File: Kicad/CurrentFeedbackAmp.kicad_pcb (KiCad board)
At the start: 2 copper layers, 200 x 100 mm, 123 parts, among them J1 Test_Etapa_3_Inf, J10 Protecc_Sup_In1, J11 Protecc_Inf_In1, J12 Protecc_Sup_In2, J13 Test_Etapa_3_Inf, J14 Entrada, J15 Salida masa2, J16 Salida tierra, J17 Salida senal, J2 Test_Realim_Out, J3 Salida masa1, J4 Protecc_Sup_Out, J5 Protecc_Inf_Out, J6 Conector Vcc, J7 Conector Vdd, J8 Test_Etapa_3_Inf, J9 Test_Etapa_3_Sup, Q1 TIP42C, Q10 BC858, Q11 BC848, Q12 BC858, Q13 BC559, Q14 BC559, Q15 BC559, Q16 BC549, Q17 BC549, Q18 BC549, Q19 BC559, Q2 BD135, Q20 BC549, Q21 BC559, Q22 BC549, Q23 BC848, Q24 BD136, Q25 BC858, Q26 BC848, Q27 BC848, Q28 BC848, Q29 BC858, Q3 BD136, Q30 BC858, Q31 BC848, Q32 BC858, Q33 BD135, Q34 TIP41C, Q35 BC858, Q36 BC848, Q37 BC848, Q38 BC848, Q4 BC848, Q40 BC858, Q41 BC858, Q5 BC848, Q6 BC858, Q7 BC858, Q8 BC848, Q9 BC858, U1 LM7812_TO220, U2 TL082, U3 LM7912_TO220, U4 LM7805_TO220, U5 LM7905_TO220

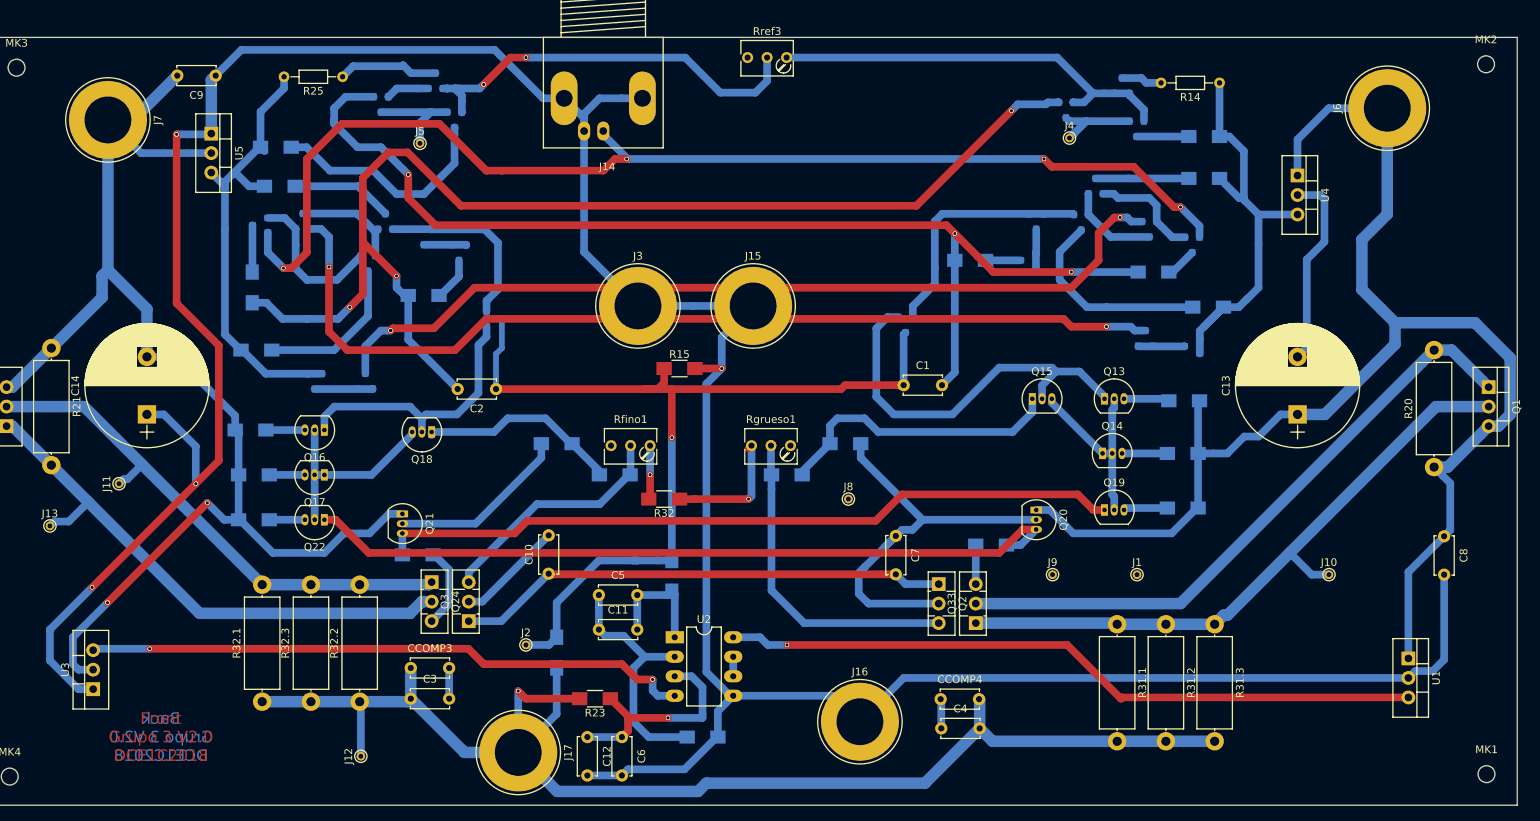
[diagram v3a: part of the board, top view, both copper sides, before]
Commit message: Avance con ensanchado, acomodado de pistas y reposicionamiento de los LM
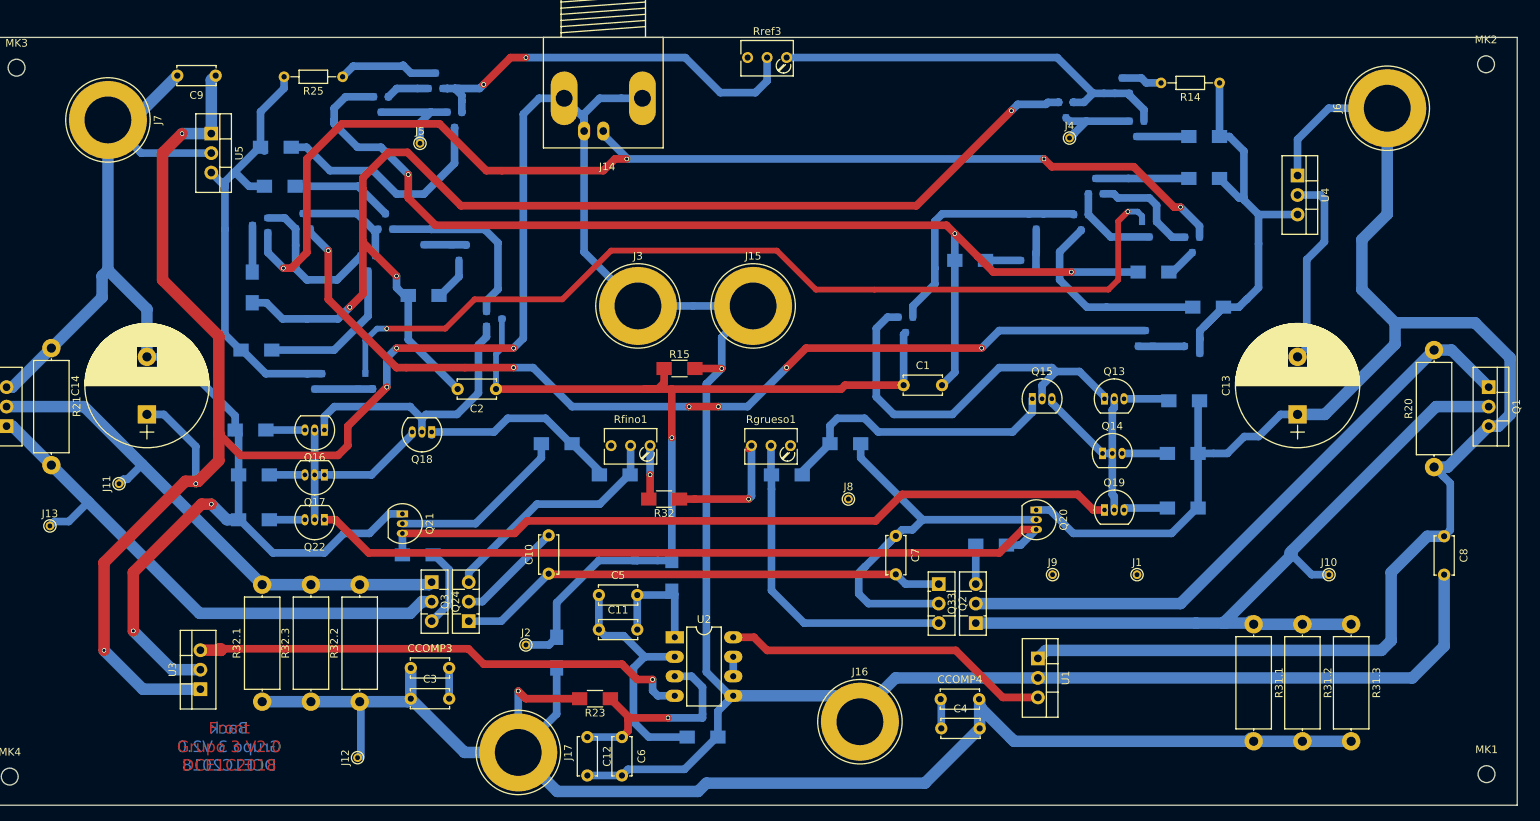
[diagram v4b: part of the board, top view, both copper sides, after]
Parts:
- moved U1 48.3 mm to (140.7, 93.8)
- moved R31.1 17.8 mm to (168.8, 89.3)
- moved R31.2 17.8 mm to (175.1, 89.3)
- moved R31.3 17.8 mm to (181.5, 89.3)
- moved U3 14.0 mm to (31.6, 97.8)
- moved J12 0.47 mm to (52.1, 106.7)
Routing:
- net GND: track 436.7 -> 489.2 mm, vias 4 -> 7
- net VccTL: track 91.3 -> 42.9 mm, vias 1 -> 0
- net Vcc: track 186.7 -> 233.6 mm
- net Vout: track 177.8 -> 197.9 mm
- net Net-(J10-Pad1): track 84.9 -> 103.5 mm
- net VddTL: track 79.2 -> 65.9 mm, vias 2 -> 1
- net Net-(Q12-Pad1): track 114.0 -> 122.1 mm, vias 3 -> 2
- net Net-(Q23-Pad1): track 124.9 -> 126.5 mm, vias 2 -> 6
- net Vdd: track 171.0 -> 171.6 mm

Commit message: Configuracion estrella
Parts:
- R10, R8, R9: moved to F.Cu
- R23: moved to B.Cu
- moved C8 33.1 mm to (183.1, 46.5), turned to 180 degrees
- moved U3 27.4 mm to (58.9, 99.6)
- moved J8 25.8 mm to (141.5, 69.1)
- moved C9 25.8 mm to (29.0, 43.2)
- moved R22 16.7 mm to (99.0, 87.4)
- moved CCOMP3 10.8 mm to (52.8, 103.9), turned to 180 degrees
- moved C3 10.5 mm to (52.8, 107.4), turned to 180 degrees
- moved R15 5.92 mm to (89.4, 59.7)
- moved C4 5.01 mm to (133.1, 102.6), turned to 180 degrees
- moved CCOMP4 5.00 mm to (133.0, 99.1), turned to 180 degrees
- moved J12 4.38 mm to (52.8, 111.0)
- moved R32.2 4.35 mm to (48.0, 98.9)
- moved R32.3 4.35 mm to (41.7, 98.9)
- moved R32.1 4.35 mm to (35.3, 98.9)
- moved J16 3.56 mm to (114.0, 102.9)
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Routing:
- net Net-(C3-Pad2): track 39.3 -> 110.7 mm, vias 0 -> 2
- net Net-(C4-Pad1): track 55.6 -> 119.6 mm, vias 0 -> 1
- net VddTL: track 65.9 -> 37.0 mm
- net Net-(J8-Pad1): track 97.2 -> 109.5 mm
- net GND: track 489.2 -> 480.2 mm, vias 7 -> 1
- net Vout: track 197.9 -> 189.4 mm, vias 1 -> 0
- net Net-(C11-Pad1): track 32.7 -> 24.8 mm
- net Net-(J1-Pad1): track 82.5 -> 87.8 mm
- net Net-(J9-Pad1): track 100.5 -> 105.0 mm
- net Net-(Q23-Pad1): track 126.5 -> 122.3 mm, vias 6 -> 2
- net Vdd: track 171.6 -> 175.1 mm, vias 2 -> 0
- net Net-(R32-Pad2): track 7.03 -> 10.4 mm
- net Ireference2: track 142.7 -> 140.2 mm
- net Net-(J11-Pad1): track 69.1 -> 71.6 mm
- net Net-(J13-Pad1): track 72.4 -> 71.1 mm
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
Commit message: 1 Unconnected, let the game begin
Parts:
- moved U5 12.2 mm to (25.9, 35.3), turned to 0 degrees
- moved U4 7.18 mm to (179.6, 35.9), turned to 180 degrees
- moved J13 5.98 mm to (17.0, 79.8)
- moved J11 5.82 mm to (23.6, 76.2)
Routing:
- net Net-(C10-Pad2): track 37.5 -> 58.4 mm
- net GND: track 480.2 -> 461.4 mm
- net Vcc: track 233.0 -> 222.7 mm
- net Net-(C4-Pad1): track 119.6 -> 123.2 mm
- net Net-(J9-Pad1): track 105.0 -> 108.6 mm
- net Vdd: track 175.1 -> 171.6 mm
- net Vdd5: track 59.7 -> 62.5 mm
- net Net-(J11-Pad1): track 71.6 -> 69.5 mm
- net Net-(Q36-Pad1): track 59.2 -> 61.1 mm, vias 2 -> 0
- net Net-(J10-Pad1): track 103.5 -> 104.8 mm
- net Vout: track 189.4 -> 188.8 mm
- net Net-(R32-Pad1): track 17.9 -> 17.4 mm
- net Net-(J8-Pad1): track 109.5 -> 108.9 mm
- net Vin+: track 152.8 -> 152.9 mm, vias 4 -> 3
- net VccTL: vias 0 -> 1
